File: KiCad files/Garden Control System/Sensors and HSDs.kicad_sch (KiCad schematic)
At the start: 0 parts

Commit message: working on power arch
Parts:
- added R13, R15, R3: R_Shunt, symbol Device:R_Shunt
- added U3: DRV8848, Package_SO:TSSOP-16-1EP_4.4x5mm_P0.65mm, symbol Driver_Motor:DRV8848
- added U4: INA4180A2IPWR, PW14_TEX, symbol INA4180A21PWR:INA4180A2IPWR
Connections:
- new net +3.3V: U4.4 (VS)
- new net GND: U3.13 (GND), U3.17 (GND), U4.11 (GND)
- new net I_SENSE0_+: R3.2, U4.3 (IN+1)
- new net I_SENSE0_-: R3.3, U4.2 (IN-1)
- new net I_SENSE1_+: R13.2, U4.5 (IN+2)
- new net I_SENSE1_-: R13.3, U4.6 (IN-2)
- new net I_SENSE2_+: R15.2, U4.10 (IN+3)
- new net I_SENSE2_-: R15.3, U4.9 (IN-3)
- new net I_SENSE3_+: U4.12 (IN+4)
- new net I_SENSE3_-: U4.13 (IN-4)
- new net M0_IN: R3.4
- new net M0_PWM: U3.16 (AIN1)
- new net M1_IN: R13.4
- new net M1_PWM: U3.15 (AIN2)
- new net M2_IN: R15.4
- new net M2_PWM: U3.9 (BIN1)
- new net MCU_I_SENSE0: U4.1 (OUT1)
- new net MCU_I_SENSE1: U4.7 (OUT2)
- new net MCU_I_SENSE2: U4.8 (OUT3)
- new net MCU_I_SENSE3: U4.14 (OUT4)
- new net SHUNT0_IN: R3.1, U3.2 (AOUT1)
- new net SHUNT1_IN: R13.1, U3.4 (AOUT2)
- new net SHUNT2_IN: R15.1, U3.7 (BOUT1)
- new net VBAT: U3.12 (VM)
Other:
- note added: "CHECK FOR CAP FILTERING"
- note added: "Current and Power Monitoring"
- note added: "Fan and Pump Driver"
- note added: "NEED TO SIZE SHUNTS PROPERLY"

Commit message: working on gate driver circuit for motor control
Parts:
- removed U3: DRV8848, Package_SO:TSSOP-16-1EP_4.4x5mm_P0.65mm, symbol Driver_Motor:DRV8848
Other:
- note added: "CHECK LAYOUT DETAILS ADD FILTERS FOR AO SIGNALS?"
- note added: "CHECK LAYOUT DETAILS TO FINISH"
- note removed: "CHECK FOR CAP FILTERING"
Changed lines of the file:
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@@
-	(wire
-		(pts
-			(xy 45.72 86.36) (xy 52.07 86.36)
-		)
-		(stroke
-			(width 0)
-			(type default)
-		)
-	)
 	(wire
 		(pts
@@
 	(wire
 		(pts
-			(xy 67.31 64.77) (xy 67.31 68.58)
+			(xy 69.85 78.74) (xy 69.85 82.55)
 		)
 		(stroke
@@
 	(wire
 		(pts
-			(xy 45.72 83.82) (xy 52.07 83.82)
-		)
-		(stroke
-			(width 0)
-			(type default)
-		)
-	)
-	(wire
-		(pts
 			(xy 149.86 107.95) (xy 147.32 107.95)
 		)
@@
 	(wire
 		(pts
-			(xy 82.55 88.9) (xy 91.44 88.9)
-		)
-		(stroke
-			(width 0)
-			(type default)
-		)
-	)
-	(wire
-		(pts
 			(xy 170.18 80.01) (xy 176.53 80.01)
 		)
@@
 	(wire
 		(pts
-			(xy 82.55 78.74) (xy 91.44 78.74)
-		)
-		(stroke
-			(width 0)
-			(type default)
-		)
-	)
-	(wire
-		(pts
 			(xy 147.32 107.95) (xy 147.32 115.57)
 		)
@@
 	(wire
 		(pts
-			(xy 67.31 99.06) (xy 67.31 102.87)
+			(xy 69.85 113.03) (xy 69.85 116.84)
 		)
 		(stroke
@@
 	(wire
 		(pts
-			(xy 45.72 91.44) (xy 52.07 91.44)
-		)
-		(stroke
-			(width 0)
-			(type default)
-		)
-	)
-	(wire
-		(pts
 			(xy 187.96 107.95) (xy 185.42 107.95)
-		)
-		(stroke
-			(width 0)
-			(type default)
-		)
-	)
-	(wire
-		(pts
-			(xy 82.55 81.28) (xy 91.44 81.28)
 		)
 		(stroke
@@
 		)
 	)
-	(text_box "Current/Voltage monitoring ICs\nDigital with I2C:INA3221AIRGVR (3 CHANNEL) ~$6\nAnalog output: INA4180A2IPWR 4channel $1.5\nAnalog output: INA2180A1IDGKR 2channel $0.9\n\nFor analog option, might need to filter before micro..\nReview datasheet\n\nHigh side current sense above motor driver."
+	(text_box "Current/Voltage monitoring ICs\nDigital with I2C:INA3221AIRGVR (3 CHANNEL) ~$6\nAnalog output: INA4180A2IPWR 4channel $1.5\nAnalog output: INA2180A1IDGKR 2channel $0.9\n\nFor analog option, might need to filter before micro..\nReview datasheet\n\nHigh side current sense above motor but below driver."
 		(exclude_from_sim no)
 		(at 148.59 29.21 0)
@@
 		)
 	)
-	(text_box "Chose to use an HBridge driver instead of \nimplenenting my own mosfet driver circuit due to \nreduced costs, ease of design, easier layout, and \nmore compact design. \n\nCould add redundancy by driving 2 outputs connected in \nparallel across 2 ICs.\n\nMotor driver connected as a HSD."
+	(text_box "Chose to use an HBridge driver instead of \nimplenenting my own mosfet driver circuit due to \nreduced costs, ease of design, easier layout, and \nmore compact design. \n\nCould add redundancy by driving 2 outputs connected in \nparallel across 2 ICs.\n\nMotor driver connected as a HSD.\n18V max motor driver DRV8848PWPR: $3.50\n48V max motor driver DRV8434PPWPR: 6.06\n\nCould do a gate driver + mosfet for 12V and 24V operation.\nMosfet: 4x IRLML6344TRPBF, $0.519 + 2x UCC27624DR (or UCC27624QDRQ1) $2.15: TOT=~$6\n(gate driver could be hooked up to 5V if \nfet Rds on is low enough at Vgs=5V. Downgrade the gate driver if so.)"
 		(exclude_from_sim no)
-		(at 45.72 29.21 0)
-		(size 45.72 26.67)
+		(at 22.86 29.21 0)
+		(size 91.44 36.83)
 		(stroke
 			(width 0)
@@
 		)
 	)
-	(text "CHECK FOR CAP FILTERING"
+	(text "CHECK LAYOUT DETAILS\nADD FILTERS FOR AO SIGNALS?"
 		(exclude_from_sim no)
 		(at 196.342 57.15 0)
+		(effects
+			(font
+				(size 1.27 1.27)
+				(color 255 0 0 1)
+			)
+		)
+	)
+	(text "CHECK LAYOUT DETAILS TO FINISH"
+		(exclude_from_sim no)
+		(at 96.774 76.2 0)
 		(effects
 			(font
@@
 	(text "NEED TO SIZE SHUNTS PROPERLY"
 		(exclude_from_sim no)
-		(at 187.452 103.378 0)
+		(at 197.612 102.87 0)
 		(effects
 			(font
@@
 	(global_label "SHUNT1_IN"
 		(shape input)
-		(at 91.44 81.28 0)
-		(fields_autoplaced yes)
-		(effects
-			(font
-				(size 1.27 1.27)
-			)
-			(justify left)
-		)
-		(property "Intersheetrefs" "${INTERSHEET_REFS}"
-			(at 104.7062 81.28 0)
+		(at 95.25 92.71 0)
+		(fields_autoplaced yes)
+		(effects
+			(font
+				(size 1.27 1.27)
+			)
+			(justify left)
+		)
+		(property "Intersheetrefs" "${INTERSHEET_REFS}"
+			(at 108.5162 92.71 0)
 			(effects
 				(font
@@
 	(global_label "M2_PWM"
 		(shape input)
-		(at 45.72 91.44 180)
+		(at 41.91 99.06 180)
 		(fields_autoplaced yes)
 		(effects
@@
 		)
 		(property "Intersheetrefs" "${INTERSHEET_REFS}"
-			(at 34.9335 91.44 0)
+			(at 31.1235 99.06 0)
 			(effects
 				(font
@@
 	(global_label "M0_PWM"
 		(shape input)
-		(at 45.72 83.82 180)
+		(at 41.91 91.44 180)
 		(fields_autoplaced yes)
 		(effects
@@
 		)
 		(property "Intersheetrefs" "${INTERSHEET_REFS}"
-			(at 34.9335 83.82 0)
+			(at 31.1235 91.44 0)
 			(effects
 				(font
@@
 	(global_label "M1_PWM"
 		(shape input)
-		(at 45.72 86.36 180)
+		(at 41.91 93.98 180)
 		(fields_autoplaced yes)
 		(effects
@@
 		)
 		(property "Intersheetrefs" "${INTERSHEET_REFS}"
-			(at 34.9335 86.36 0)
+			(at 31.1235 93.98 0)
 			(effects
 				(font
@@
 	(global_label "SHUNT0_IN"
 		(shape input)
-		(at 91.44 78.74 0)
-		(fields_autoplaced yes)
-		(effects
-			(font
-				(size 1.27 1.27)
-			)
-			(justify left)
-		)
-		(property "Intersheetrefs" "${INTERSHEET_REFS}"
-			(at 104.7062 78.74 0)
+		(at 95.25 90.17 0)
+		(fields_autoplaced yes)
+		(effects
+			(font
+				(size 1.27 1.27)
+			)
+			(justify left)
+		)
+		(property "Intersheetrefs" "${INTERSHEET_REFS}"
+			(at 108.5162 90.17 0)
 			(effects
 				(font
@@
 	(global_label "SHUNT2_IN"
 		(shape input)
-		(at 91.44 88.9 0)
-		(fields_autoplaced yes)
-		(effects
-			(font
-				(size 1.27 1.27)
-			)
-			(justify left)
-		)
-		(property "Intersheetrefs" "${INTERSHEET_REFS}"
-			(at 104.7062 88.9 0)
+		(at 95.25 100.33 0)
+		(fields_autoplaced yes)
+		(effects
+			(font
+				(size 1.27 1.27)
+			)
+			(justify left)
+		)
+		(property "Intersheetrefs" "${INTERSHEET_REFS}"
+			(at 108.5162 100.33 0)
 			(effects
 				(font
@@
 	(symbol
 		(lib_id "power:GND")
-		(at 67.31 102.87 0)
+		(at 69.85 116.84 0)
 		(unit 1)
 		(exclude_from_sim no)
@@
 		(fields_autoplaced yes)
 		(property "Reference" "#PWR031"
-			(at 67.31 109.22 0)
+			(at 69.85 123.19 0)
 			(effects
 				(font
@@
 		)
 		(property "Value" "GND"
-			(at 67.31 107.95 0)
+			(at 69.85 121.92 0)
 			(effects
 				(font
@@
 		)
 		(property "Footprint" ""
-			(at 67.31 102.87 0)
+			(at 69.85 116.84 0)
 			(effects
 				(font
@@
 		)
 		(property "Datasheet" ""
-			(at 67.31 102.87 0)
+			(at 69.85 116.84 0)
 			(effects
 				(font
@@
 		)
 		(property "Description" "Power symbol creates a global label with name \"GND\" , ground"
-			(at 67.31 102.87 0)
+			(at 69.85 116.84 0)
 			(effects
 				(font
@@
 	(symbol
 		(lib_id "power:VBUS")
-		(at 67.31 64.77 0)
+		(at 69.85 78.74 0)
 		(unit 1)
 		(exclude_from_sim no)
@@
 		(dnp no)
 		(property "Reference" "#PWR038"
-			(at 67.31 68.58 0)
+			(at 69.85 82.55 0)
 			(effects
 				(font
@@
 		)
 		(property "Value" "VBAT"
-			(at 65.532 60.96 0)
+			(at 68.072 74.93 0)
 			(effects
 				(font
@@
 		)
 		(property "Footprint" ""
-			(at 67.31 64.77 0)
+			(at 69.85 78.74 0)
 			(effects
 				(font
@@
 		)
 		(property "Datasheet" ""
-			(at 67.31 64.77 0)
+			(at 69.85 78.74 0)
 			(effects
 				(font
@@
 		)
 		(property "Description" ""
-			(at 67.31 64.77 0)
+			(at 69.85 78.74 0)
 			(effects
 				(font
@@
 					(unit 1)
 				)
-			)
-		)
-	)
-	(symbol
-		(lib_id "Driver_Motor:DRV8848")
-		(at 67.31 83.82 0)
-		(unit 1)
-		(exclude_from_sim no)
-		(in_bom yes)
-		(on_board yes)
-		(dnp no)
-		(fields_autoplaced yes)
-		(property "Reference" "U3"
-			(at 69.5041 66.04 0)
-			(effects
-				(font
-					(size 1.27 1.27)
-				)
-				(justify left)
-			)
-		)
-		(property "Value" "DRV8848"
-			(at 69.5041 68.58 0)
-			(effects
-				(font
-					(size 1.27 1.27)
-				)
-				(justify left)
-			)
-		)
-		(property "Footprint" "Package_SO:TSSOP-16-1EP_4.4x5mm_P0.65mm"
-			(at 67.31 101.6 0)
-			(effects
-				(font
-					(size 1.27 1.27)
-				)
-				(hide yes)
-			)
-		)
-		(property "Datasheet" "http://www.ti.com/lit/ds/symlink/drv8848.pdf"
-			(at 38.1 49.53 0)
-			(effects
-				(font
-					(size 1.27 1.27)
-				)
-				(hide yes)
-			)
-		)
-		(property "Description" "Dual H-Bridge motor driver, PWM controlled, single/dual brushed DC stepper, +2 to +18 VDD, TSSOP-16"
-			(at 67.31 83.82 0)
-			(effects
-				(font
-					(size 1.27 1.27)
-				)
-				(hide yes)
-			)
-		)
-		(pin "15"
-		)
-		(pin "11"
-		)
-		(pin "6"
-		)
-		(pin "1"
-		)
-		(pin "2"
-		)
-		(pin "12"
-		)
-		(pin "14"
-		)
-		(pin "10"
-		)
-		(pin "16"
-		)
-		(pin "3"
-		)
-		(pin "17"
-		)
-		(pin "4"
-		)
-		(pin "5"
-		)
-		(pin "13"
-		)
-		(pin "7"
-		)
-		(pin "8"
-		)
-		(pin "9"
-		)
-		(instances
-			(project "Garden Control System"
-				(path "/be495e14-3da3-4129-8396-1871cb6cba29/9f2dbd4f-9250-47a2-9054-c36b37ba7178"
-					(reference "U3")
-					(unit 1)
-				)

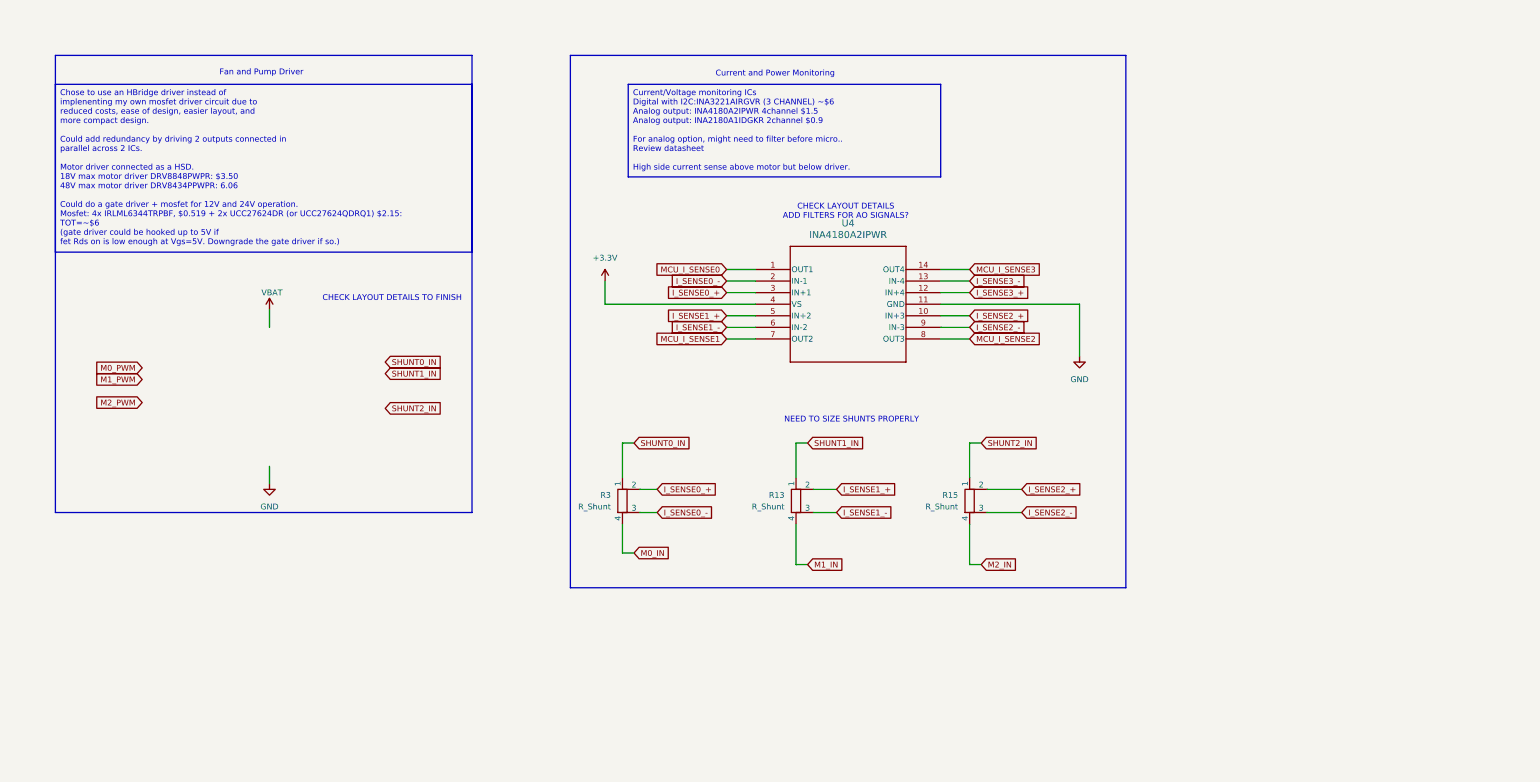
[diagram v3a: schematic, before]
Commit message: expanded power supply section. completed LSD design. sized shunt resistors
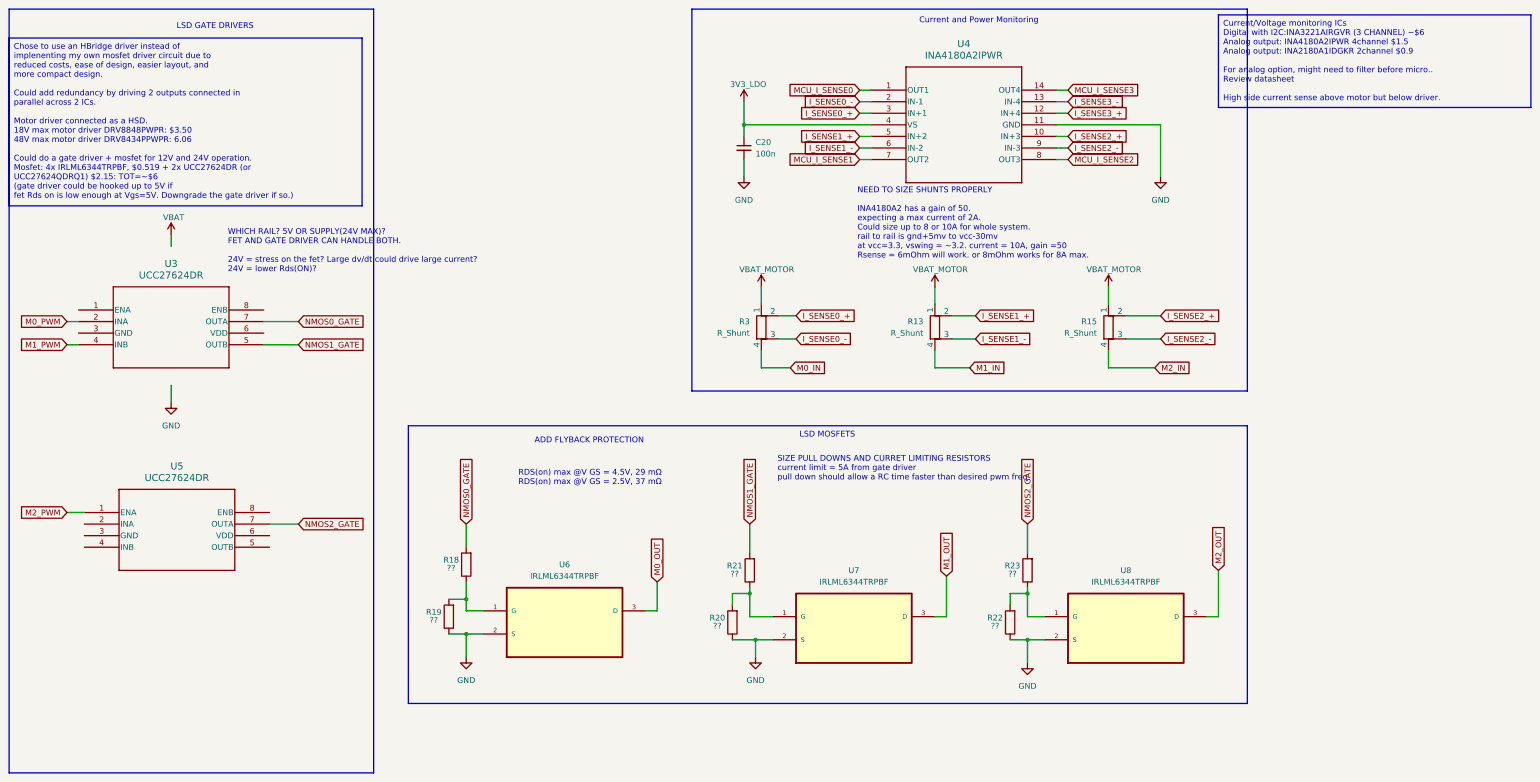
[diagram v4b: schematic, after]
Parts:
- added C20: 100n, symbol Device:C_Small
- added R18, R19, R20, R21, R22, R23: ??, symbol Device:R
- added U3, U5: UCC27624DR, SOIC_D0008A_TEX, symbol UCC27624DR:UCC27624DR
- added U6, U7, U8: IRLML6344TRPBF, IRLML6344TRPBF:SOT95P240X112-3N, symbol IRLML6344TRPBF:IRLML6344TRPBF
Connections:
- net SHUNT1_IN is gone; now on net VBAT_MOTOR: R13.1
- net SHUNT2_IN is gone; now on net VBAT_MOTOR: R15.1
- net GND: now also C20.2, R19.1, R20.1, R22.1, U6.2 (S), U7.2 (S), U8.2 (S)
- net M0_PWM: now also U3.2 (INA)
- net M1_PWM: now also U3.4 (INB)
- net M2_PWM: now also U5.1 (ENA)
- net +3.3V renamed 3V3_LDO
- net 3V3_LDO: now also C20.1
- net SHUNT0_IN renamed VBAT_MOTOR
- new net: R18.1, R19.2, U6.1 (G)
- new net: R22.2, R23.1, U8.1 (G)
- new net: R20.2, R21.1, U7.1 (G)
- new net M0_OUT: U6.3 (D)
- new net M1_OUT: U7.3 (D)
- new net M2_OUT: U8.3 (D)
- new net NMOS0_GATE: R18.2, U3.7 (OUTA)
- new net NMOS1_GATE: R21.2, U3.5 (OUTB)
- new net NMOS2_GATE: R23.2, U5.7 (OUTA)
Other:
- note added: "ADD FLYBACK PROTECTION"
- note added: "LSD GATE DRIVERS"
- note added: "LSD MOSFETS"
- note added: "NEED TO SIZE SHUNTS PROPERLY INA4180A2 has a gain of 50. expecting a max current of 2A. Could size up to 8 or 10A for whole system. rail to rail is gnd+5mv to vcc-30mv at vcc=3.3, vswing = ~3.2. current = 10A, gain =50 Rsense = 6mOhm will work. or 8mOhm works for 8A max."
- note added: "RDS(on) max @V GS = 4.5V, 29 mΩ RDS(on) max @V GS = 2.5V, 37 mΩ"
- note added: "SIZE PULL DOWNS AND CURRET LIMITING RESISTORS current limit = 5A from gate driver pull down should allow a RC time faster than desired pwm freq"
- note added: "WHICH RAIL? 5V OR SUPPLY(24V MAX)? FET AND GATE DRIVER CAN HANDLE BOTH. 24V = stress on the fet? Large dv/dt could drive large current? 24V = lower Rds(ON)?"
- note removed: "CHECK LAYOUT DETAILS ADD FILTERS FOR AO SIGNALS?"
- note removed: "CHECK LAYOUT DETAILS TO FINISH"
- note removed: "Fan and Pump Driver"
- note removed: "NEED TO SIZE SHUNTS PROPERLY"
- moved on the sheet: R13, R15, R3, U4

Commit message: adding recent schematic progress
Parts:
- added C42, C45: 100n, symbol Device:C_Small
- added C43, C44: 10u, symbol Device:C_Small
- added R24, R25, R26: 221, symbol Device:R
- R13, R15, R3: value R_Shunt -> 30m
- R18, R21, R23: value ?? -> 22.1
- R19, R20, R22: value ?? -> 510k
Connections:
- net GND: now also U3.3 (GND), U5.3 (GND), C42.2, C43.2, C44.2, C45.2
- net M0_PWM: now also R24.1; no longer U3.2 (INA)
- net M1_PWM: now also R25.1; no longer U3.4 (INB)
- net M2_PWM: now also R26.1; no longer U5.1 (ENA)
- net at U5.2 (INA): now also R26.2
- net 5V_BUCK: now reaches U5.6 (VDD)
- net 5V_BUCK: now also U3.6 (VDD), C42.1, C43.1, C44.1, C45.1
- net at U5.8 (ENB): now also U5.1 (ENA)
- net at U3.1 (ENA): now also U3.8 (ENB)
- net 3V3_LDO renamed 3V3
- new net: R25.2, U3.4 (INB)
- new net: R24.2, U3.2 (INA)
- no-connect marks 0 -> 2
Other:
- note added: "Current limiting resistors for micro: Pins are rated for 25mA. Ill choose to limit to 15mA R = 3.3/0.015 = ~220. Next closest E common series value is 221ohms"
- note added: "For the best high-speed circuit performance and to prevent noise problems because the device draws current from the VDD pin to bias all internal circuits, use two VDD bypass capacitors. Also, use surface mount, low ESR capacitors. A 0.1-μF ceramic capacitor should be located less than 1 mm from the VDD to GND pins of the gate-driver device. In addition, a larger capacitor (≥1 μF) must be connecte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"
- note added: "INA4180A2 has a gain of 50. expecting a max current of 2A on motors and 8A through VBAT. Could size up to 8A for whole system. rail to rail is gnd+5mv to vcc-30mv at vcc=3.3, vswing = ~3.2. Iin =8A,Imotor =2, gain =50 Rsense = Vswing/GxImax = 3.2/50x8 = 8mOhm. Rsense_in = 8mOhm will work for Vout = 0.005-3.2V Rsense_motor = 30mOhm will work for Motor current sense 0.005-3V"
- note added: "SIZE PULL DOWNS AND CURRET LIMITING RESISTORS current limit = 5A from gate driver pull down should allow a RC time faster than desired pwm freq. Community suggests above 15KHz to remove audiable noise and as low as possible to reduce switching losses. Sizing for 50KHz and can reduce speed through FW as needed. Cgd + Cgs = ~700pF, V = 5V, Rgate = 22.1 (using same resistor as driver input Resistor)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"
- note added: "Supply 3.3V from buck and Vdd from Vin UCC21550BDWR"
- note added: "Tie enable to pullup? 3v3? Micro Pin?"
- note removed: "NEED TO SIZE SHUNTS PROPERLY INA4180A2 has a gain of 50. expecting a max current of 2A. Could size up to 8 or 10A for whole system. rail to rail is gnd+5mv to vcc-30mv at vcc=3.3, vswing = ~3.2. current = 10A, gain =50 Rsense = 6mOhm will work. or 8mOhm works for 8A max."
- note removed: "SIZE PULL DOWNS AND CURRET LIMITING RESISTORS current limit = 5A from gate driver pull down should allow a RC time faster than desired pwm freq"
- note removed: "WHICH RAIL? 5V OR SUPPLY(24V MAX)? FET AND GATE DRIVER CAN HANDLE BOTH. 24V = stress on the fet? Large dv/dt could drive large current? 24V = lower Rds(ON)?"
- moved on the sheet: R13, R15, R18, R19, R3, U3, U5, U6
